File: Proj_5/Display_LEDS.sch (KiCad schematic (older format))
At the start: 3 parts

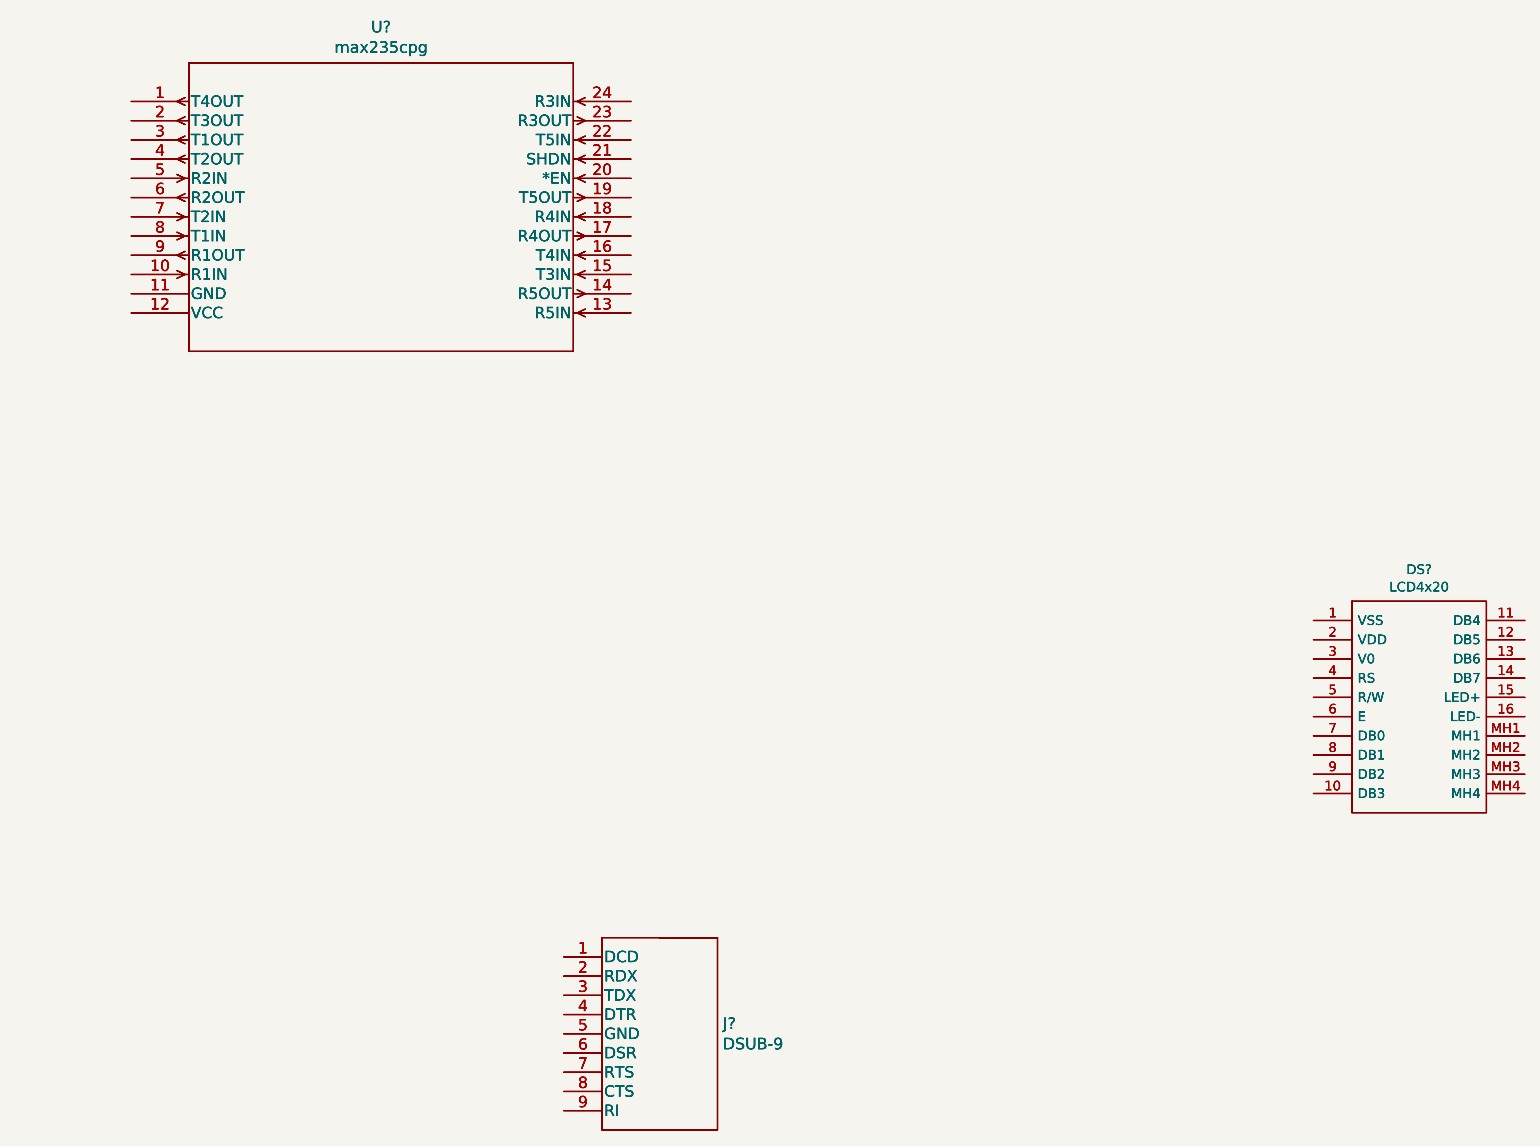
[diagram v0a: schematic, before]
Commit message: Added address decoding
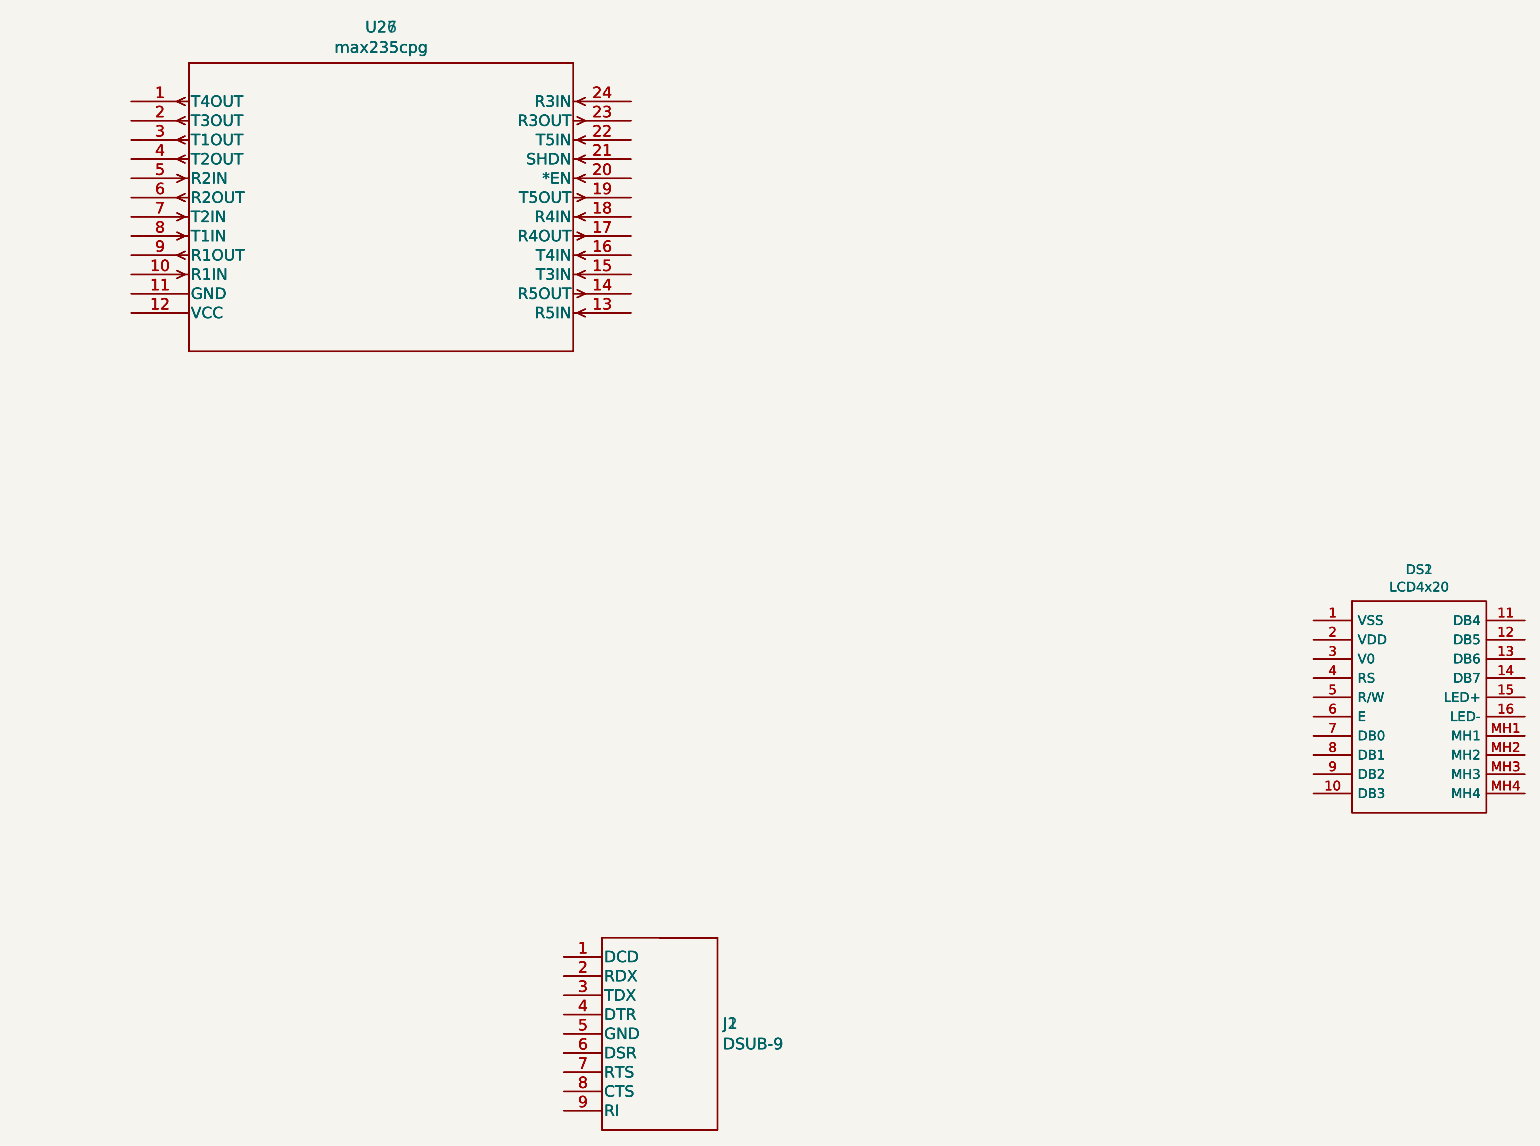
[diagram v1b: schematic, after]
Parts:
- removed DS?: LCD4x20, LCD4x20, symbol LCD4x20:LCD4x20
- removed J?: DSUB-9, DSUB-9, symbol DSUB-9:DSUB-9
- removed U?: max235cpg, max235cpg, symbol max235cpg:max235cpg
- added DS1, DS2: LCD4x20, LCD4x20, symbol LCD4x20:LCD4x20
- added J1, J2: DSUB-9, DSUB-9, symbol DSUB-9:DSUB-9
- added U26, U27: max235cpg, max235cpg, symbol max235cpg:max235cpg
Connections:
- new net: U26.1 (T4OUT), U27.1 (T4OUT)
- new net: U26.10 (R1IN), U27.10 (R1IN)
- new net: U26.11 (GND), U27.11 (GND)
- new net: U26.12 (VCC), U27.12 (VCC)
- new net: U26.13 (R5IN), U27.13 (R5IN)
- new net: U26.14 (R5OUT), U27.14 (R5OUT)
- new net: U26.15 (T3IN), U27.15 (T3IN)
- new net: U26.16 (T4IN), U27.16 (T4IN)
- new net: U26.17 (R4OUT), U27.17 (R4OUT)
- new net: U26.18 (R4IN), U27.18 (R4IN)
- new net: U26.19 (T5OUT), U27.19 (T5OUT)
- new net: U26.2 (T3OUT), U27.2 (T3OUT)
- new net: U26.20 (*EN), U27.20 (*EN)
- new net: U26.21 (SHDN), U27.21 (SHDN)
- new net: U26.22 (T5IN), U27.22 (T5IN)
- new net: U26.23 (R3OUT), U27.23 (R3OUT)
- new net: U26.24 (R3IN), U27.24 (R3IN)
- new net: U26.3 (T1OUT), U27.3 (T1OUT)
- new net: U26.4 (T2OUT), U27.4 (T2OUT)
- new net: U26.5 (R2IN), U27.5 (R2IN)
- new net: U26.6 (R2OUT), U27.6 (R2OUT)
- new net: U26.7 (T2IN), U27.7 (T2IN)
- new net: U26.8 (T1IN), U27.8 (T1IN)
- new net: U26.9 (R1OUT), U27.9 (R1OUT)
- new net: DS1.1 (VSS), DS2.1 (VSS)
- new net: DS1.10 (DB3), DS2.10 (DB3)
- new net: DS1.11 (DB4), DS2.11 (DB4)
- new net: DS1.12 (DB5), DS2.12 (DB5)
- new net: DS1.13 (DB6), DS2.13 (DB6)
- new net: DS1.14 (DB7), DS2.14 (DB7)
- new net: DS1.15 (LED+), DS2.15 (LED+)
- new net: DS1.16 (LED-), DS2.16 (LED-)
- new net: DS1.2 (VDD), DS2.2 (VDD)
- new net: DS1.3 (V0), DS2.3 (V0)
- new net: DS1.4 (RS), DS2.4 (RS)
- new net: DS1.5 (R/W), DS2.5 (R/W)
- new net: DS1.6 (E), DS2.6 (E)
- new net: DS1.7 (DB0), DS2.7 (DB0)
- new net: DS1.8 (DB1), DS2.8 (DB1)
- new net: DS1.9 (DB2), DS2.9 (DB2)
- new net: DS1.MH1, DS2.MH1
- new net: DS1.MH2, DS2.MH2
- new net: DS1.MH3, DS2.MH3
- new net: DS1.MH4, DS2.MH4
- new net: J1.1 (DCD), J2.1 (DCD)
- new net: J1.2 (RDX), J2.2 (RDX)
- new net: J1.3 (TDX), J2.3 (TDX)
- new net: J1.4 (DTR), J2.4 (DTR)
- new net: J1.5 (GND), J2.5 (GND)
- new net: J1.6 (DSR), J2.6 (DSR)
- new net: J1.7 (RTS), J2.7 (RTS)
- new net: J1.8 (CTS), J2.8 (CTS)
- new net: J1.9 (RI), J2.9 (RI)
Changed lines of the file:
@@
 $EndDescr
 $Comp
-L max235cpg:max235cpg U?
+L max235cpg:max235cpg U26
 U 1 1 5EAF79CF
 P 6100 3900
-F 0 "U?" H 7400 4287 60  0000 C CNN
+F 0 "U26" H 7400 4287 60  0000 C CNN
 F 1 "max235cpg" H 7400 4181 60  0000 C CNN
 F 2 "max235cpg" H 7400 4140 60  0001 C CNN
@@
 $EndComp
 $Comp
-L LCD4x20:LCD4x20 DS?
+L LCD4x20:LCD4x20 DS1
 U 1 1 5EAFDAD4
 P 12250 6600
-F 0 "DS?" H 12800 6865 50  0000 C CNN
+F 0 "DS1" H 12800 6865 50  0000 C CNN
 F 1 "LCD4x20" H 12800 6774 50  0000 C CNN
 F 2 "LCD4x20" H 13200 6700 50  0001 L CNN
@@
 $EndComp
 $Comp
-L DSUB-9:DSUB-9 J?
+L DSUB-9:DSUB-9 J1
 U 1 1 5EAFF563
 P 8350 8350
-F 0 "J?" H 9178 8003 60  0000 L CNN
+F 0 "J1" H 9178 8003 60  0000 L CNN
 F 1 "DSUB-9" H 9178 7897 60  0000 L CNN
 F 2 "DSUB-9" H 8950 7990 60  0001 C CNN
@@
 $EndComp
 $Comp
-L max235cpg:max235cpg U?
-U 1 1 5EAF79CF
+L max235cpg:max235cpg U27
+U 1 1 5F18FC44
 P 6100 3900
-F 0 "U?" H 7400 4287 60  0000 C CNN
+F 0 "U27" H 7400 4287 60  0000 C CNN
 F 1 "max235cpg" H 7400 4181 60  0000 C CNN
 F 2 "max235cpg" H 7400 4140 60  0001 C CNN
@@
 $EndComp
 $Comp
-L LCD4x20:LCD4x20 DS?
-U 1 1 5EAFDAD4
+L LCD4x20:LCD4x20 DS2
+U 1 1 5F18FC45
 P 12250 6600
-F 0 "DS?" H 12800 6865 50  0000 C CNN
+F 0 "DS2" H 12800 6865 50  0000 C CNN
 F 1 "LCD4x20" H 12800 6774 50  0000 C CNN
 F 2 "LCD4x20" H 13200 6700 50  0001 L CNN
@@
 $EndComp
 $Comp
-L DSUB-9:DSUB-9 J?
-U 1 1 5EAFF563
+L DSUB-9:DSUB-9 J2
+U 1 1 5F18FC46
 P 8350 8350
-F 0 "J?" H 9178 8003 60  0000 L CNN
+F 0 "J2" H 9178 8003 60  0000 L CNN
 F 1 "DSUB-9" H 9178 7897 60  0000 L CNN
 F 2 "DSUB-9" H 8950 7990 60  0001 C CNN

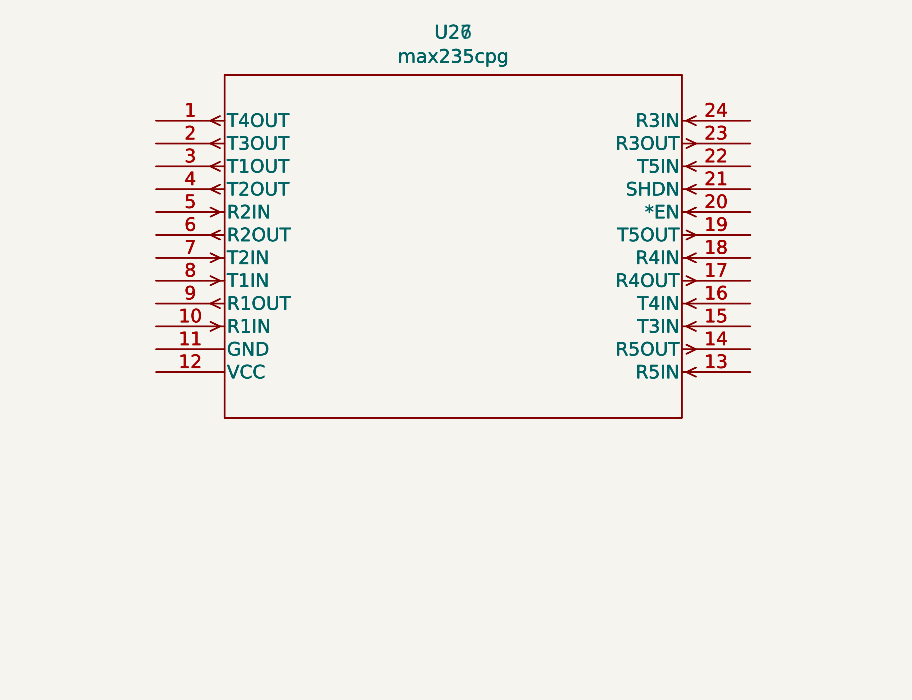
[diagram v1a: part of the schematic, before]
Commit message: Added Caps to Each Vcc per desc.
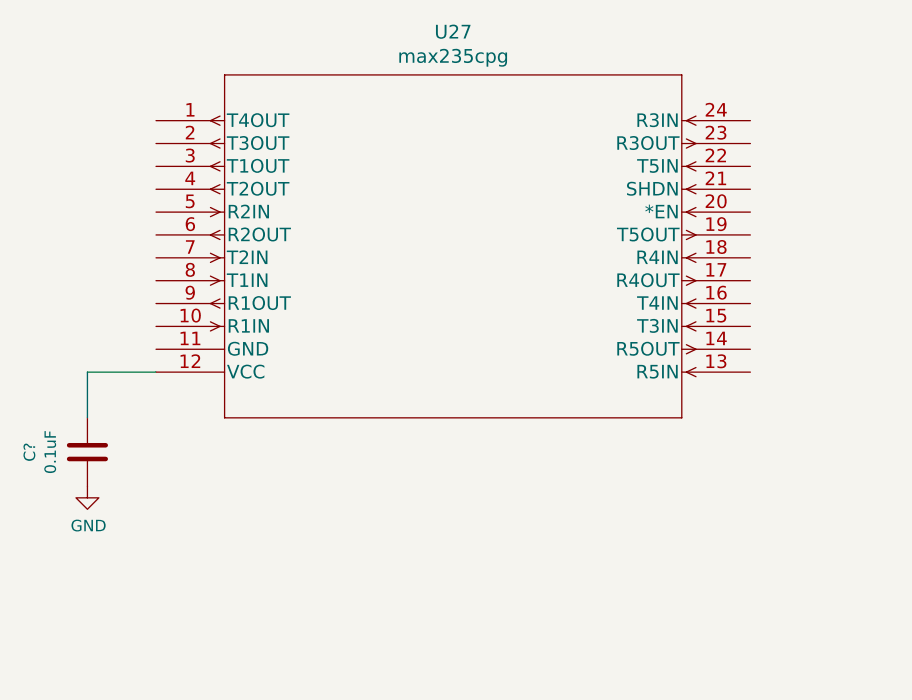
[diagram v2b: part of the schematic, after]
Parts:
- removed U26: max235cpg, max235cpg, symbol max235cpg:max235cpg
- added C?: 0.1uF, symbol Device:C
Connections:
- net at U27.12 (VCC): now also C?.1
- new net GND: C?.2
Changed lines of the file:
@@
 $Descr A2 23386 16535
 encoding utf-8
-Sheet 11 11
+Sheet 10 11
 Title ""
 Date ""
@@
 Comment4 ""
 $EndDescr
-$Comp
-L max235cpg:max235cpg U26
-U 1 1 5EAF79CF
-P 6100 3900
-F 0 "U26" H 7400 4287 60  0000 C CNN
-F 1 "max235cpg" H 7400 4181 60  0000 C CNN
-F 2 "max235cpg" H 7400 4140 60  0001 C CNN
-F 3 "" H 6100 3900 60  0000 C CNN
-	1    6100 3900
-	1    0    0    -1
-$EndComp
 $Comp
 L LCD4x20:LCD4x20 DS1
@@
 	1    0    0    -1
 $EndComp
+$Comp
+L Device:C C?
+U 1 1 5EA6A56C
+P 5800 5350
+AR Path="/5EA98353/5EA6A56C" Ref="C?"  Part="1"
+AR Path="/5EAF7226/5EA6A56C" Ref="C?"  Part="1"
+F 0 "C?" V 5548 5350 50  0000 C CNN
+F 1 "0.1uF" V 5639 5350 50  0000 C CNN
+F 2 "" H 5838 5200 50  0001 C CNN
+F 3 "~" H 5800 5350 50  0001 C CNN
+	1    5800 5350
+	1    0    0    -1
+$EndComp
+Wire Wire Line
+	5800 5200 5800 5000
+Wire Wire Line
+	5800 5000 6100 5000
+$Comp
+L power:GND #PWR?
+U 1 1 5EAAD1B7
+P 5800 5500
+F 0 "#PWR?" H 5800 5250 50  0001 C CNN
+F 1 "GND" H 5805 5327 50  0000 C CNN
+F 2 "" H 5800 5500 50  0001 C CNN
+F 3 "" H 5800 5500 50  0001 C CNN
+	1    5800 5500
+	1    0    0    -1
+$EndComp
